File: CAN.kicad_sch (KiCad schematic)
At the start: 8 parts, among them J14 Screw_Terminal_01x03, J7 8P8C_Shielded, J8 8P8C_Shielded, SW2 SW_DIP_x01, U2 SIT65HVD230DR

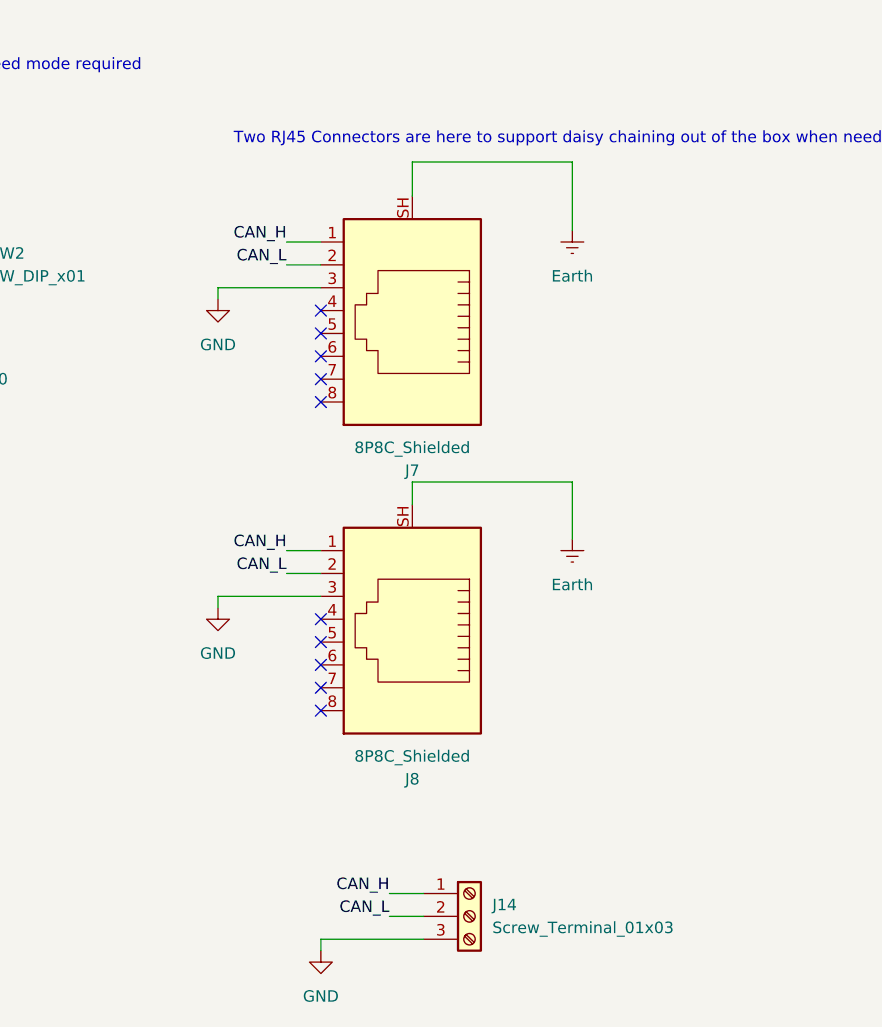
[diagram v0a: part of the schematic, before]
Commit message: Key CHanges for connector choices , termination and semi-final decisions on them
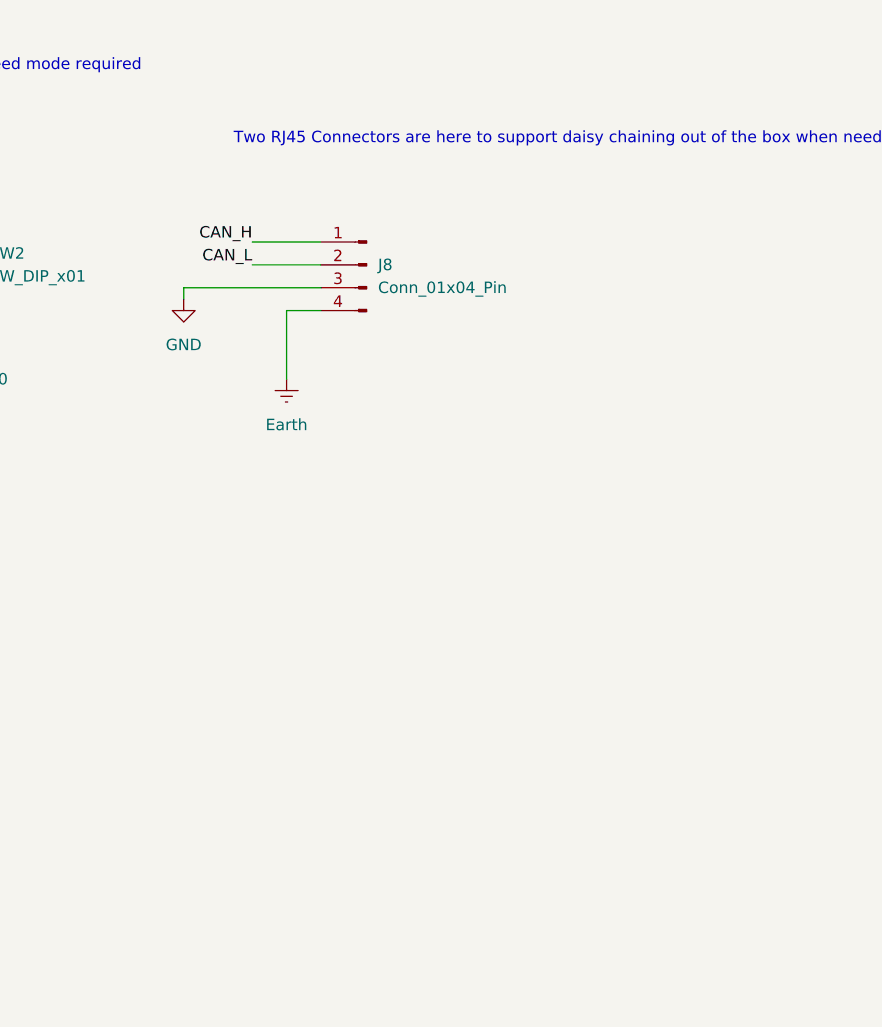
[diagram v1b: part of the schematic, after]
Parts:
- removed J14: Screw_Terminal_01x03, TerminalBlock_Phoenix:TerminalBlock_Phoenix_PT-1,5-3-3.5-H_1x03_P3.50mm_Horizontal, symbol Connector:Screw_Terminal_01x03
- removed J7, J8: 8P8C_Shielded, Connector_RJ:RJ45_Ninigi_GE, symbol Connector:8P8C_Shielded
- added J8: Conn_01x04_Pin, Connector_JST:JST_XH_B4B-XH-A_1x04_P2.50mm_Vertical, symbol Connector:Conn_01x04_Pin
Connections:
- net CAN_H: now also J8.1 (Pin_1)
- net CAN_L: now also J8.2 (Pin_2)
- net Earth: now also J8.4 (Pin_4)
- net GND: now also J8.3 (Pin_3)
- no-connect marks 11 -> 1

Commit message: Done routing for Buck Converter , Rs485 and CAN , Some Routing for MCU and associated circuitry , NO ETHERNET ROUTING , NO module Interconnects yet
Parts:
- R9: footprint Resistor_SMD:R_0805_2012Metric -> Resistor_SMD:R_1210_3225Metric
- SW2: footprint Button_Switch_THT:SW_DIP_SPSTx01_Slide_6.7x4.1mm_W7.62mm_P2.54mm_LowProfile -> Button_Switch_SMD:SW_DIP_SPSTx01_Slide_6.7x4.1mm_W8.61mm_P2.54mm_LowProfile
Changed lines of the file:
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@@
 			)
 		)
-		(property "Footprint" "Resistor_SMD:R_0805_2012Metric"
+		(property "Footprint" "Resistor_SMD:R_1210_3225Metric"
 			(at 165.862 85.09 90)
 			(effects
@@
 			)
 		)
-		(property "Footprint" "Button_Switch_THT:SW_DIP_SPSTx01_Slide_6.7x4.1mm_W7.62mm_P2.54mm_LowProfile"
+		(property "Footprint" "Button_Switch_SMD:SW_DIP_SPSTx01_Slide_6.7x4.1mm_W8.61mm_P2.54mm_LowProfile"
 			(at 154.94 73.66 0)
 			(effects

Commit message: Added Base
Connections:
- net CAN_H: now also SW2.1; no longer SW2.2
- net at R9.1: now also SW2.2; no longer SW2.1
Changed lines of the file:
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@@
 		(lib_id "Switch:SW_DIP_x01")
 		(at 167.64 73.66 90)
+		(mirror x)
 		(unit 1)
 		(exclude_from_sim no)
@@
 		(dnp no)
 		(property "Reference" "SW2"
-			(at 171.45 72.3899 90)
+			(at 171.45 74.9301 90)
 			(effects
 				(font
@@
 		)
 		(property "Value" "SW_DIP_x01"
-			(at 171.45 74.9299 90)
+			(at 171.45 72.3901 90)
 			(effects
 				(font

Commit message: UPDATED
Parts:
- C16: footprint Capacitor_SMD:C_0805_2012Metric -> Capacitor_SMD:C_1206_3216Metric_Pad1.33x1.80mm_HandSolder
- J8: footprint Connector_JST:JST_XH_B4B-XH-A_1x04_P2.50mm_Vertical -> Connector_JST:JST_XH_S4B-XH-A_1x04_P2.50mm_Horizontal
- R8: footprint Resistor_SMD:R_0805_2012Metric -> Resistor_SMD:R_1206_3216Metric_Pad1.30x1.75mm_HandSolder
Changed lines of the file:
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@@
 			)
 		)
-		(property "Footprint" "Capacitor_SMD:C_0805_2012Metric"
+		(property "Footprint" "Capacitor_SMD:C_1206_3216Metric_Pad1.33x1.80mm_HandSolder"
 			(at 77.1652 85.09 0)
 			(effects
@@
 			)
 		)
-		(property "Footprint" "Connector_JST:JST_XH_B4B-XH-A_1x04_P2.50mm_Vertical"
+		(property "Footprint" "Connector_JST:JST_XH_S4B-XH-A_1x04_P2.50mm_Horizontal"
 			(at 213.36 73.66 0)
 			(effects
@@
 					(size 1.27 1.27)
 				)
-				(hide yes)
 			)
 		)
@@
 			)
 		)
-		(property "Footprint" "Resistor_SMD:R_0805_2012Metric"
+		(property "Footprint" "Resistor_SMD:R_1206_3216Metric_Pad1.30x1.75mm_HandSolder"
 			(at 140.462 78.74 90)
 			(effects
